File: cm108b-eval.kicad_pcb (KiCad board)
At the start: 2 copper layers, 60 x 50 mm, 42 parts, among them IC1 CM108B, J1 SPKR, J2 MIC, J3 RADIO_DATA, SW1 MUTE_REC, SW2 MUTE_PLAY, SW3 VOL_DN, SW4 VOL_UP

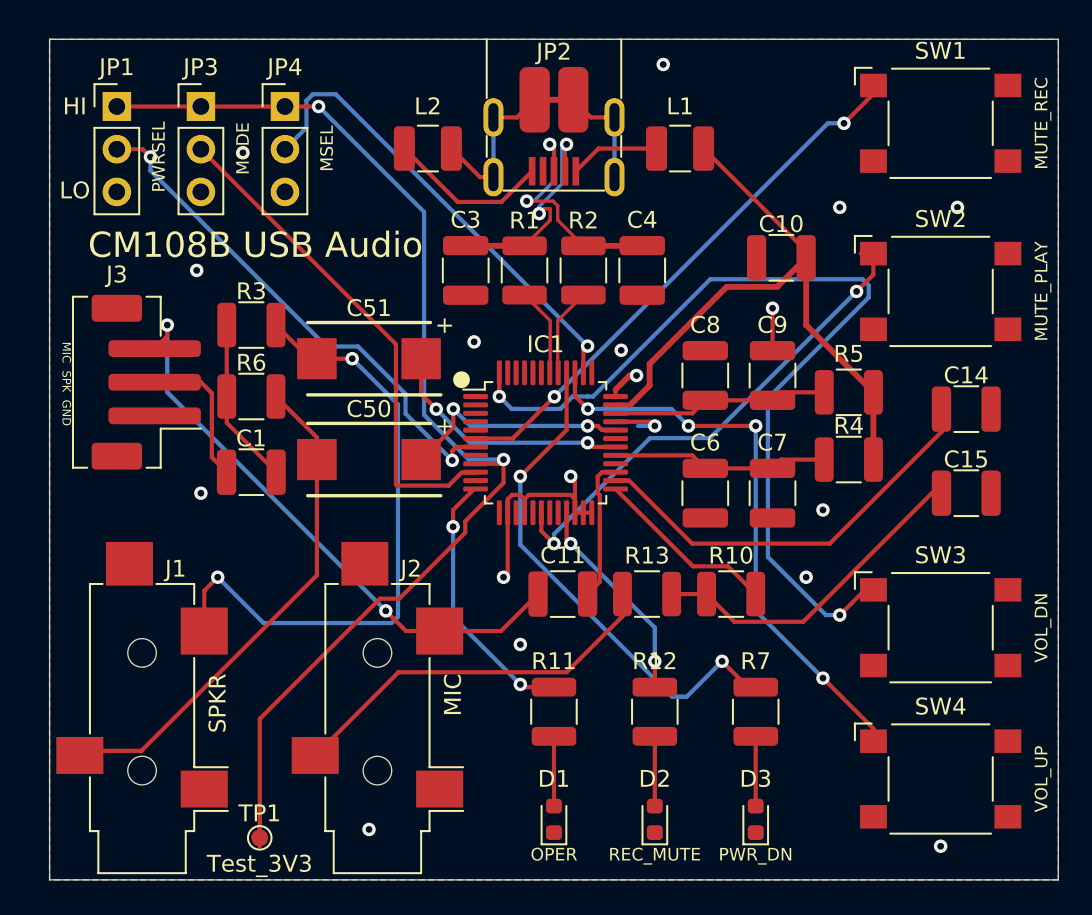
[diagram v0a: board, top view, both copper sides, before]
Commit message: Add more test points
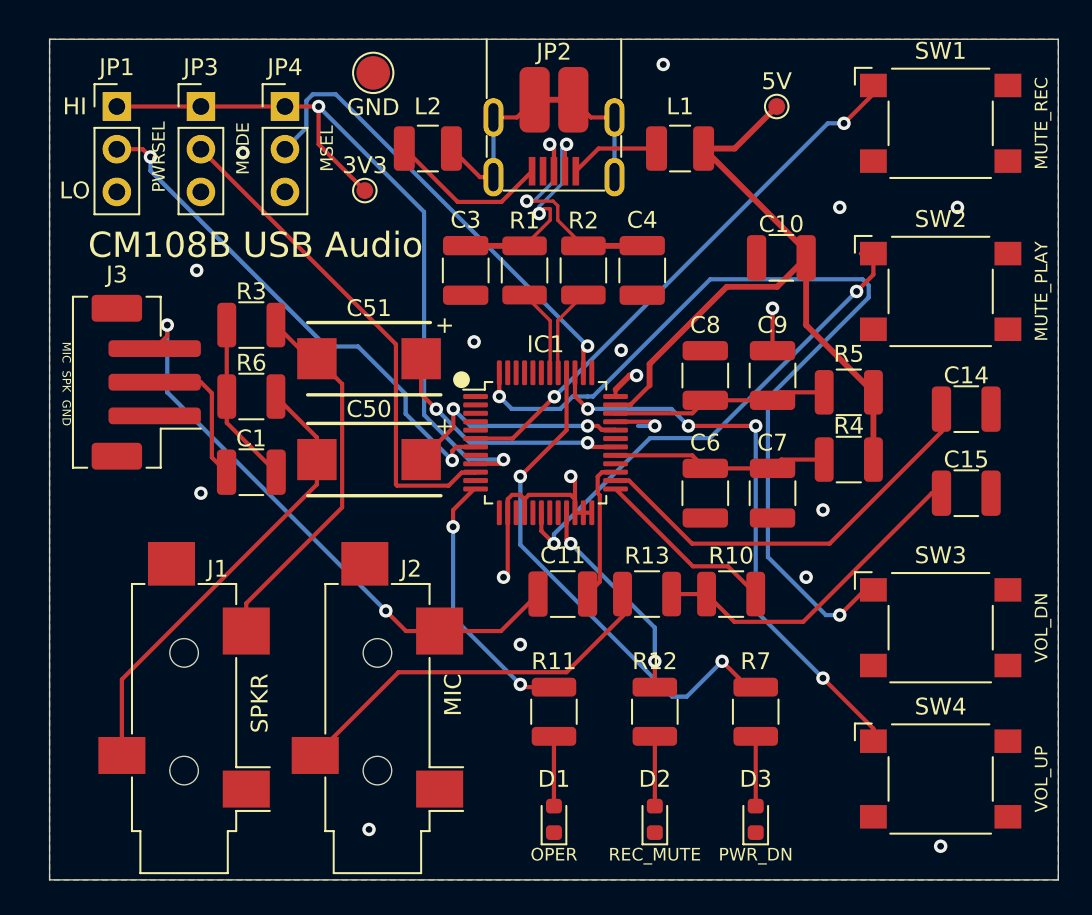
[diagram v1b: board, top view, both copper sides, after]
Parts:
- added TP1: GND, TestPoint:TestPoint_Pad_D2.0mm, F.Cu at (149.2, 72.0)
- added TP2: 5V, TestPoint:TestPoint_Pad_D1.0mm, F.Cu at (173.2, 74.0)
- TP3: renamed from TP1; value Test_3V3 -> 3V3
- moved TP3 39.0 mm to (148.8, 79.0)
- moved J1 2.50 mm to (138.0, 111.0)
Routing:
- net +3V3: track 70.2 -> 46.7 mm
- net /AUDIO_R: track 37.9 -> 22.4 mm, vias 2 -> 0
- net VBUS: track 38.4 -> 43.8 mm
- net /AUDIO_L: track 30.6 -> 27.2 mm

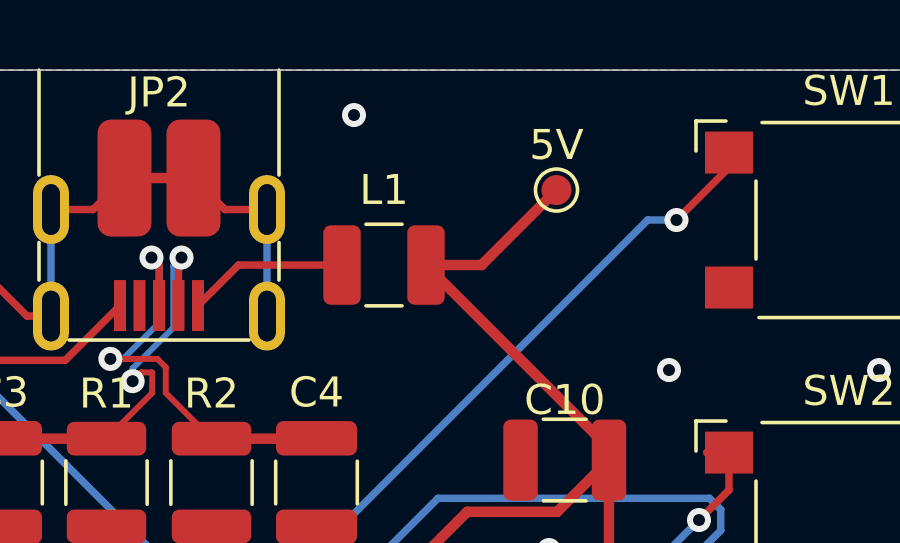
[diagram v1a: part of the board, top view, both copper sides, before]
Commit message: Move 5V test point to directly off USB
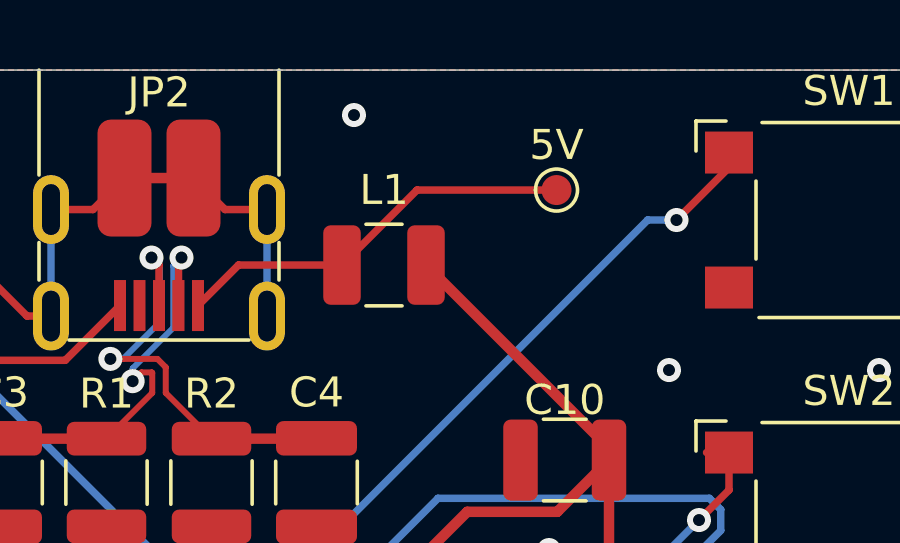
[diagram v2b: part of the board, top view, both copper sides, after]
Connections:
- TP2 pad 1: VBUS -> Net-(JP2-Pad1)
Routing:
- net Net-(JP2-Pad1): track 5.36 -> 13.5 mm
- net VBUS: track 43.8 -> 38.4 mm

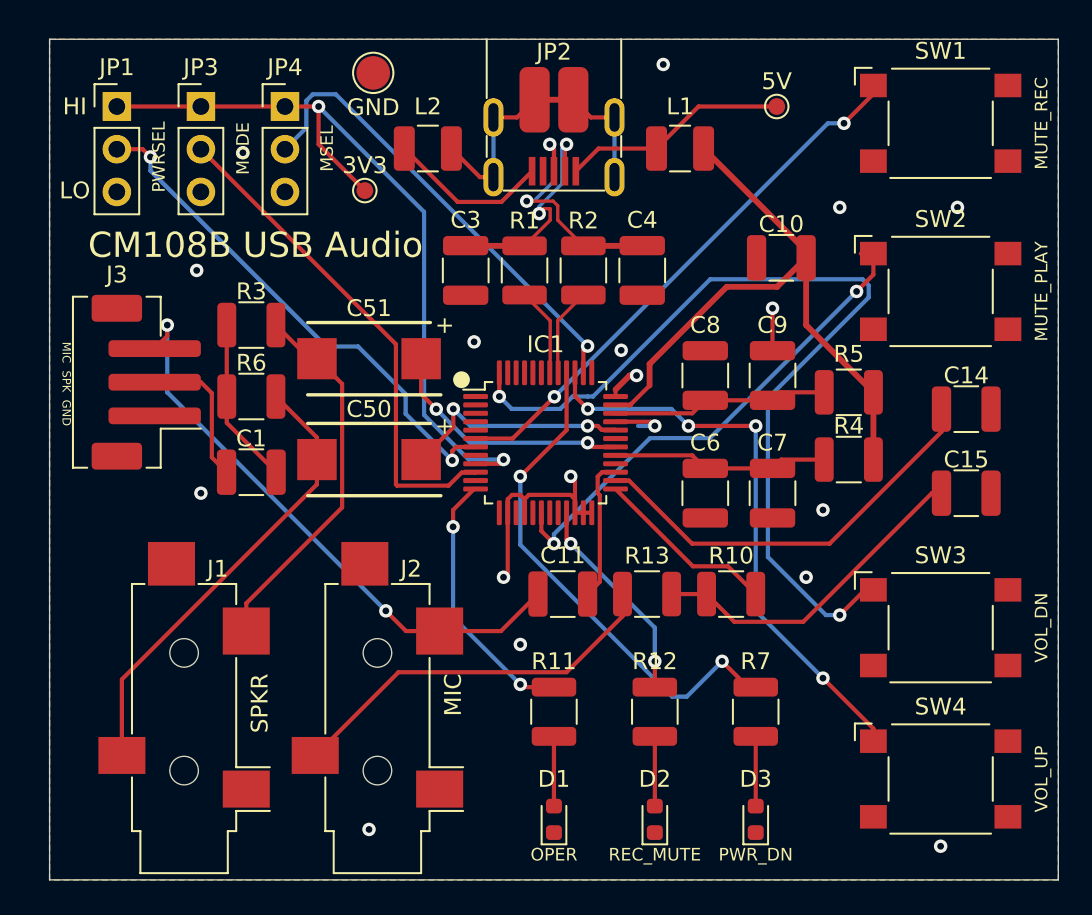
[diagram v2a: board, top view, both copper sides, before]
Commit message: Incorporate learnings from first physical prototype
* Button footprint pad numberings are wrong for symbol, so they were always pressed
* Turn J3 for solderability
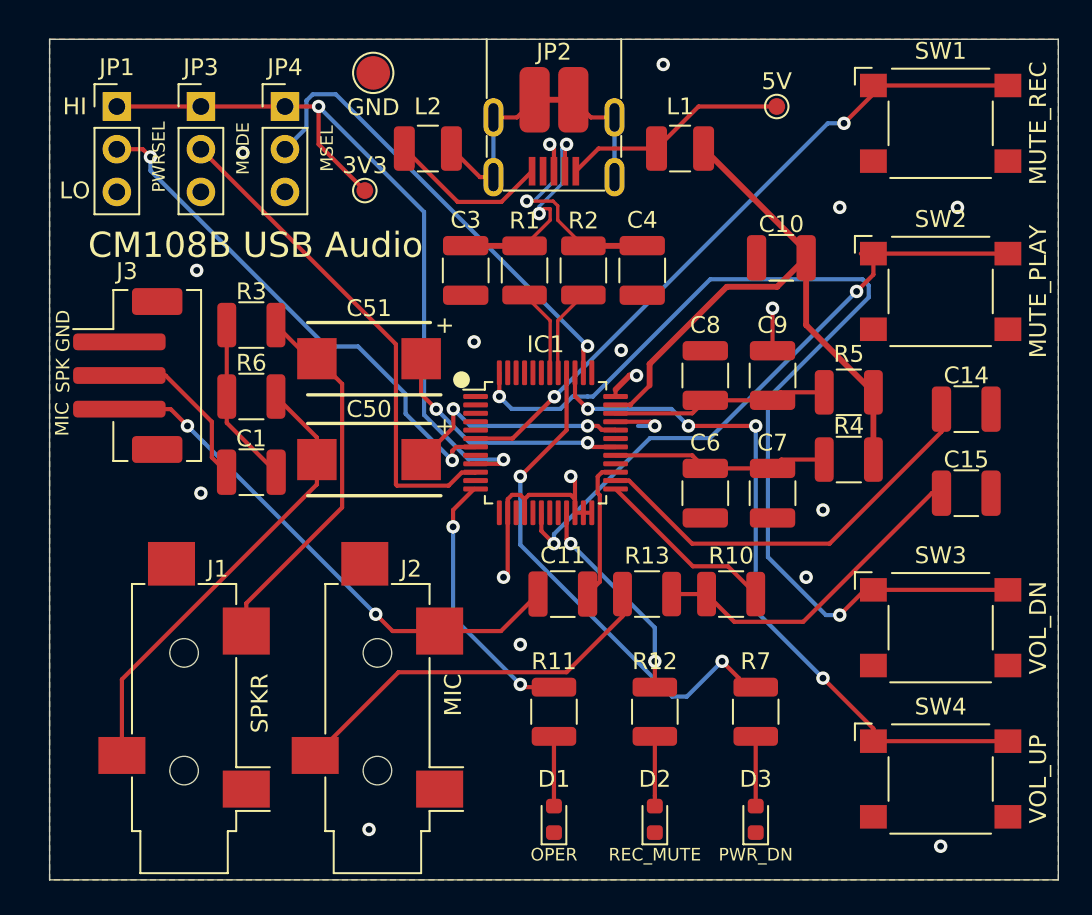
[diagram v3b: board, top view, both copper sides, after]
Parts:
- SW1, SW2, SW3, SW4: footprint Button_Switch_SMD:SW_SPST_Omron_B3FS-100xP -> Omron:SW_SPST_Omron_B3FS-100xP
- moved J3 1.17 mm to (134.7, 90.0), turned to 270 degrees
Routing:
- net /VOLUP: track 34.8 -> 42.8 mm
- net /VOLDN: track 54.3 -> 62.3 mm
- net /MUTER: track 32.7 -> 40.7 mm
- net /MUTEP: track 30.1 -> 38.1 mm
- net /MIC_IN: track 34.6 -> 31.3 mm
- net Net-(C1-Pad2): track 8.73 -> 10.0 mm
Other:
- board text added: "CM108B Audio Evaluation Board v4 C. Keller 2021-04-18 https://github.com/k0swe/cm108b-eval"
- board text removed: "CM108B Audio Evaluation Board v4 C. Keller 2021-04-14 https://github.com/k0swe/cm108b-eval"
- board text removed: "MIC SPK GND"

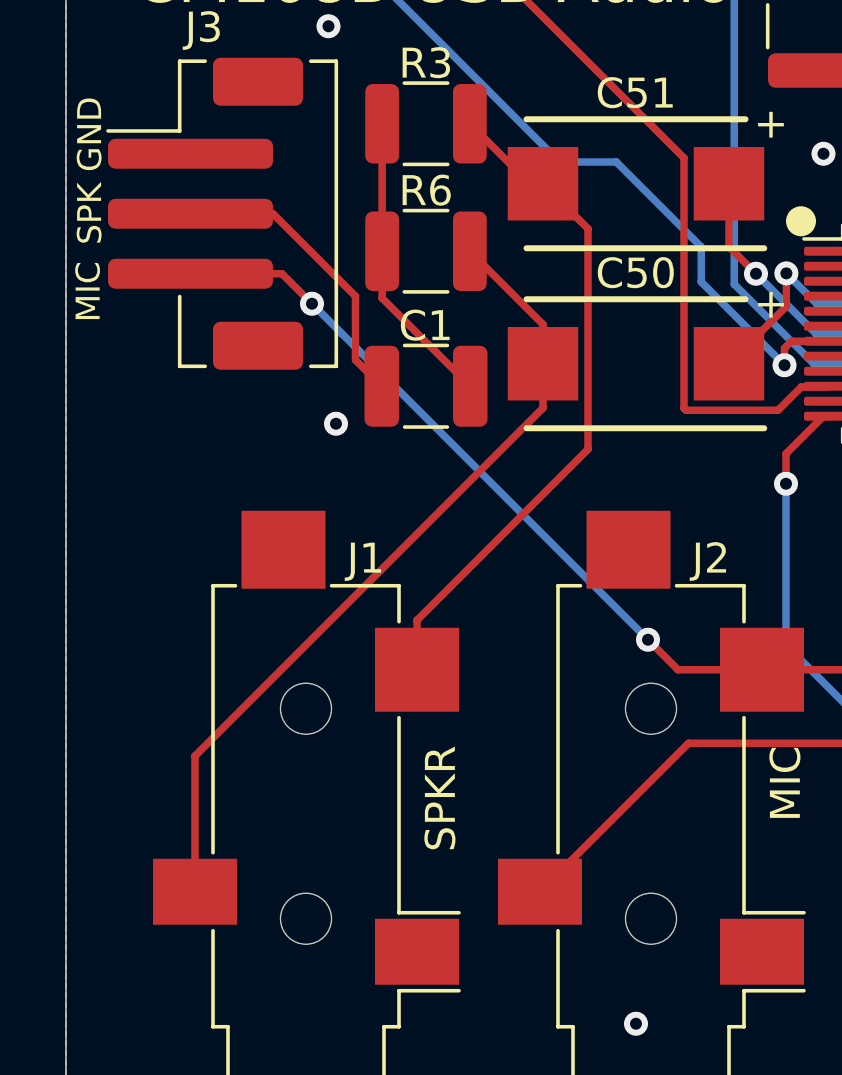
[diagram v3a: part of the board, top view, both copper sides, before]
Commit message: Fix R and L on J1
Resolves #1
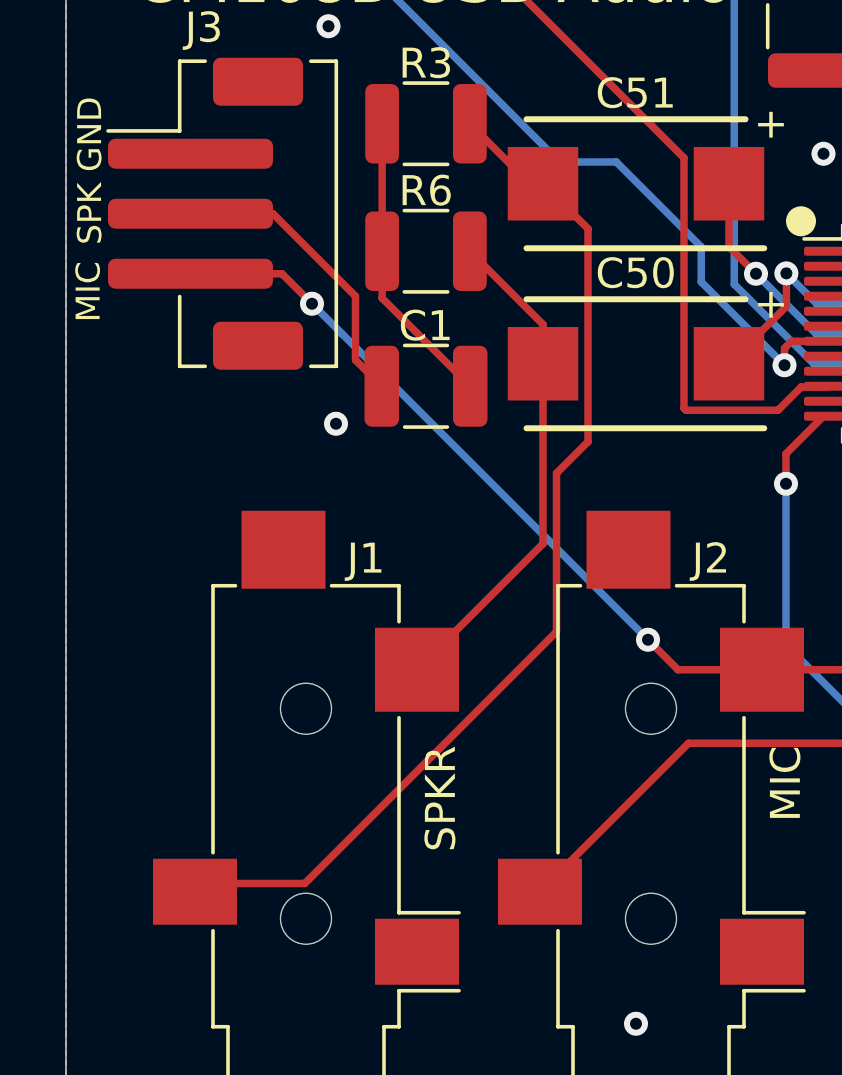
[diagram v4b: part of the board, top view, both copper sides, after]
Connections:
- J1 pad R: /AUDIO_L -> /AUDIO_R
- J1 pad T: /AUDIO_R -> /AUDIO_L
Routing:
- net /AUDIO_R: track 22.4 -> 34.9 mm
- net /AUDIO_L: track 27.2 -> 16.7 mm
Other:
- board text added: "CM108B Audio Evaluation Board v5 C. Keller 2021-04-21 https://github.com/k0swe/cm108b-eval"
- board text removed: "CM108B Audio Evaluation Board v4 C. Keller 2021-04-18 https://github.com/k0swe/cm108b-eval"
